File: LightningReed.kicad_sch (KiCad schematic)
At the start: 175 parts, among them P1 Conn_WallPlug, Q1 NCE65T180D, Q10 DMZ6005E, Q11 2N7002K, Q12 NCEP15T14D, Q13 BSS123, Q2 2N7002, Q3 1N60G, Q4 2N7002, Q5 2N7002K, Q6 2N7002K, Q7 NCE65T260K, Q8 NCE65T260K, Q9 NCE0102, T1 Transformer_2P_2S, U1 UCC28056, U2 78L05S, U3 LMC7111, U4 UCC28780, U5 UCC27712, U6 LM317G, U7 FODM8801A, U8 TL431DBZ, U9 UCC24612-1DBV

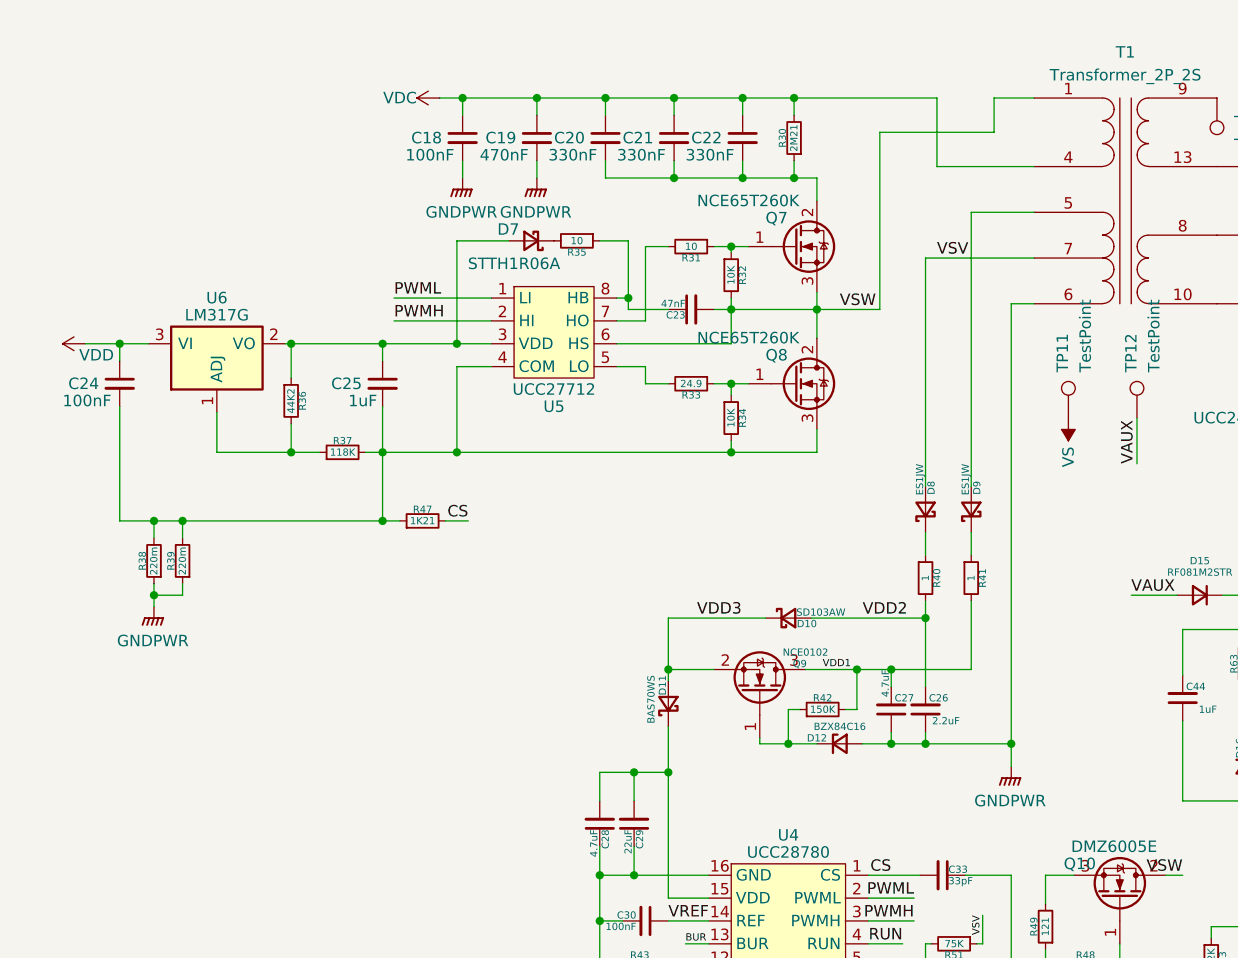
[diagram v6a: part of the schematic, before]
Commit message: Flyback controller left - layout
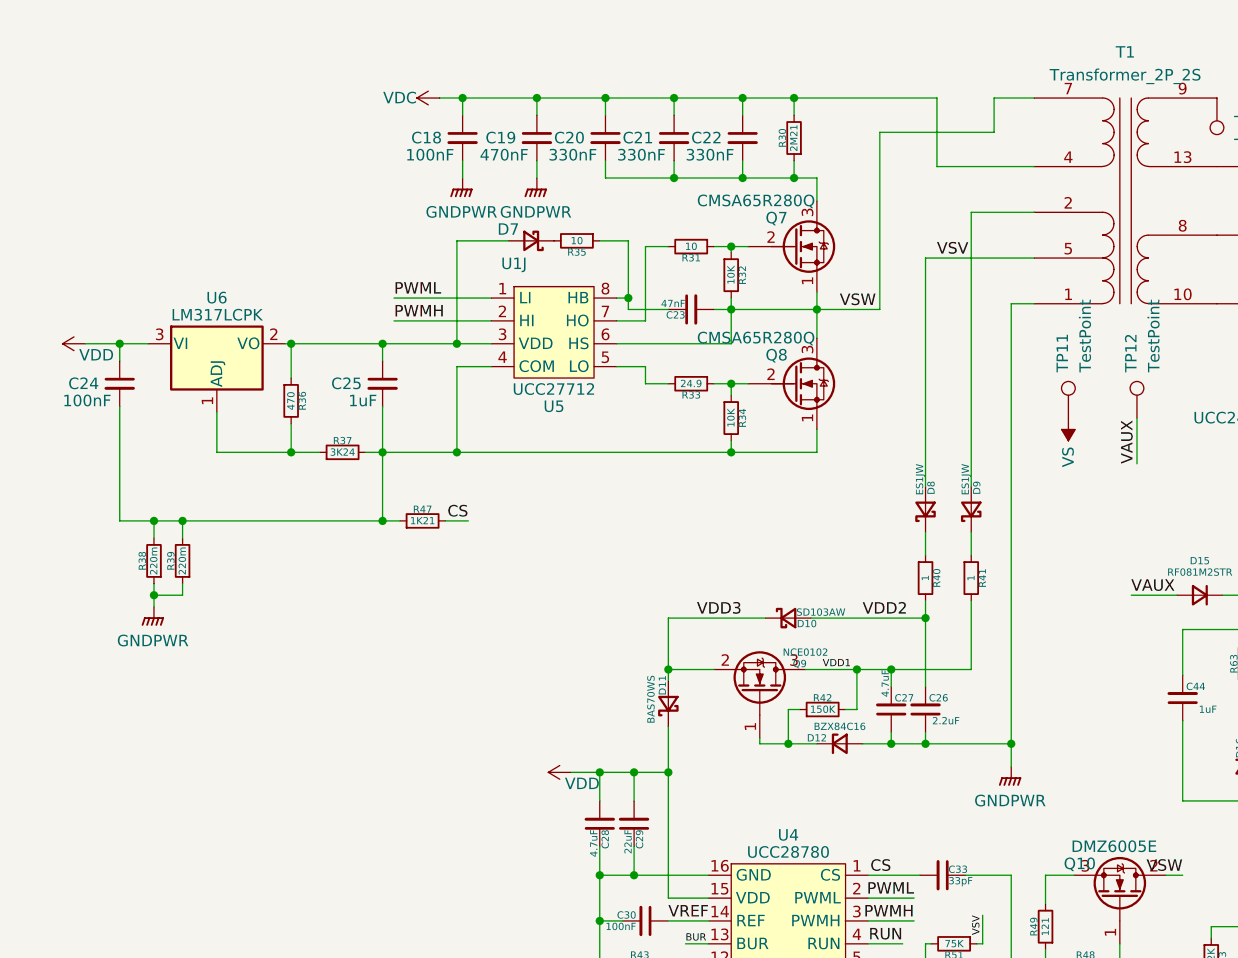
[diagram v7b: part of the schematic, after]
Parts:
- removed Q7: NCE65T260K, Package_TO_SOT_SMD:TO-252-2, symbol Device:Q_NMOS_GDS
- added Q7: CMSA65R280Q, Package_SON:VSONP-8-1EP_5x6_P1.27mm, symbol Device:Q_NMOS_SGD
- D7: value STTH1R06A -> U1J; footprint Diode_SMD:D_SMA -> Diode_SMD:D_SOD-123F
- Q8: value NCE65T260K -> CMSA65R280Q; footprint Package_TO_SOT_SMD:TO-252-2 -> Package_SON:VSONP-8-1EP_5x6_P1.27mm; symbol Device:Q_NMOS_GDS -> Device:Q_NMOS_SGD
- R36: value 44K2 -> 470
- R37: value 118K -> 3K24
- U2: footprint Package_TO_SOT_SMD:SOT-89-3 -> Package_TO_SOT_SMD:SOT-23
- U6: value LM317G -> LM317LCPK; footprint Package_TO_SOT_SMD:SOT-223-3_TabPin2 -> Package_TO_SOT_SMD:SOT-89-3; symbol Regulator_Linear:NCP1117-ADJ_SOT223 -> Regulator_Linear:LM317L_SOT-89
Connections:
- net GNDPWR: now also T1.1 (SD); no longer T1.6 (SD)
- net VDD: now also C28.2, C29.2, D11.1 (K), U4.15 (VDD)
- net VSV: now also T1.5 (SD); no longer T1.7 (SD)
- net VSW: now also Q8.3 (D), T1.7 (AA), Q7.1 (S); no longer Q8.2 (D), T1.1 (AA)
- net at R33.1, R34.1: now also Q8.2 (G); no longer Q8.1 (G)
- net at C24.2, C25.2, R34.2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: now also Q8.1 (S); no longer Q8.3 (S)
- net at C20.2, C21.2, C22.2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: now also Q7.3 (D)
- net at D9.2 (A): now also T1.2 (SC); no longer T1.5 (SC)
- net at R31.1, R32.1: now also Q7.2 (G)
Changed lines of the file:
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@@
   (junction (at 28.575 157.48) (diameter 0) (color 0 0 0 0)
   )
+  (junction (at 199.39 98.425) (diameter 0) (color 0 0 0 0)
+  )
   (junction (at 175.26 50.8) (diameter 0) (color 0 0 0 0)
   )
@@
     (stroke (width 0) (type default))
   )
+  (wire (pts (xy 196.215 98.425) (xy 199.39 98.425))
+    (stroke (width 0) (type default))
+  )
   (wire (pts (xy 271.145 78.74) (xy 271.145 82.55))
     (stroke (width 0) (type default))
@@
       (effects (font (size 1.27 1.27)))
     )
-    (property "Footprint" "Package_TO_SOT_SMD:SOT-89-3" (at 36.195 172.72 0)
+    (property "Footprint" "Package_TO_SOT_SMD:SOT-23" (at 36.195 172.72 0)
       (effects (font (size 1.27 1.27) italic) hide)
     )
@@
     )
   )
+  (symbol (lib_id "Device:Q_NMOS_SGD") (at 220.98 40.005 0) (unit 1)
+    (in_bom yes) (on_board yes) (dnp no)
+    (property "Reference" "Q7" (at 217.805 36.83 0)
+      (effects (font (size 1.27 1.27)) (justify left))
+    )
+    (property "Value" "CMSA65R280Q" (at 210.185 34.925 0)
+      (effects (font (size 1.27 1.27)) (justify left))
+    )
+    (property "Footprint" "Package_SON:VSONP-8-1EP_5x6_P1.27mm" (at 226.06 37.465 0)
+      (effects (font (size 1.27 1.27)) hide)
+    )
+    (property "Datasheet" "~" (at 220.98 40.005 0)
+      (effects (font (size 1.27 1.27)) hide)
+    )
+    (pin "1")
+    (pin "2")
+    (pin "3")
+    (instances
+      (project "LightningReed"
+        (path "/ed30a684-3009-4c45-ba04-268ec6465166"
+          (reference "Q7") (unit 1)
+        )
+      )
+    )
+  )
   (symbol (lib_id "Device:R_Small") (at 123.19 154.94 180) (unit 1)
     (in_bom yes) (on_board yes) (dnp no)
@@
     )
   )
+  (symbol (lib_id "power:VDD") (at 196.215 98.425 90) (unit 1)
+    (in_bom yes) (on_board yes) (dnp no)
+    (property "Reference" "#PWR042" (at 200.025 98.425 0)
+      (effects (font (size 1.27 1.27)) hide)
+    )
+    (property "Value" "VDD" (at 199.39 99.695 90)
+      (effects (font (size 1.27 1.27)) (justify left))
+    )
+    (property "Footprint" "" (at 196.215 98.425 0)
+      (effects (font (size 1.27 1.27)) hide)
+    )
+    (property "Datasheet" "" (at 196.215 98.425 0)
+      (effects (font (size 1.27 1.27)) hide)
+    )
+    (pin "1")
+    (instances
+      (project "LightningReed"
+        (path "/ed30a684-3009-4c45-ba04-268ec6465166"
+          (reference "#PWR042") (unit 1)
+        )
+      )
+    )
+  )
   (symbol (lib_id "Device:R_Small") (at 95.25 86.36 180) (unit 1)
     (in_bom yes) (on_board yes) (dnp no)
@@
       (effects (font (size 0.8 0.8)))
     )
-    (property "Value" "118K" (at 170.815 62.865 90)
+    (property "Value" "3K24" (at 170.815 62.865 90)
       (effects (font (size 0.8 0.8)))
     )
@@
       (effects (font (size 0.8 0.8)))
     )
-    (property "Value" "44K2" (at 165.1 57.15 90)
+    (property "Value" "470" (at 165.1 57.15 90)
       (effects (font (size 0.8 0.8)))
     )
@@
       (effects (font (size 1.27 1.27)) hide)
     )
-    (pin "1")
+    (pin "7")
     (pin "10")
     (pin "13")
     (pin "4")
+    (pin "2")
+    (pin "1")
     (pin "5")
-    (pin "6")
-    (pin "7")
     (pin "8")
     (pin "9")
@@
     )
   )
-  (symbol (lib_id "Device:Q_NMOS_GDS") (at 220.98 55.245 0) (unit 1)
+  (symbol (lib_id "Device:Q_NMOS_SGD") (at 220.98 55.245 0) (unit 1)
     (in_bom yes) (on_board yes) (dnp no)
     (property "Reference" "Q8" (at 217.805 52.07 0)
       (effects (font (size 1.27 1.27)) (justify left))
     )
-    (property "Value" "NCE65T260K" (at 210.185 50.165 0)
+    (property "Value" "CMSA65R280Q" (at 210.185 50.165 0)
       (effects (font (size 1.27 1.27)) (justify left))
     )
-    (property "Footprint" "Package_TO_SOT_SMD:TO-252-2" (at 226.06 52.705 0)
+    (property "Footprint" "Package_SON:VSONP-8-1EP_5x6_P1.27mm" (at 226.06 52.705 0)
       (effects (font (size 1.27 1.27)) hide)
     )
@@
       (effects (font (size 1.27 1.27)))
     )
-    (property "Value" "STTH1R06A" (at 189.865 41.91 0)
+    (property "Value" "U1J" (at 189.865 41.91 0)
       (effects (font (size 1.27 1.27)))
     )
-    (property "Footprint" "Diode_SMD:D_SMA" (at 191.77 39.37 90)
+    (property "Footprint" "Diode_SMD:D_SOD-123F" (at 191.77 39.37 90)
       (effects (font (size 1.27 1.27)) hide)
     )
@@
     )
   )
-  (symbol (lib_id "Regulator_Linear:NCP1117-ADJ_SOT223") (at 156.845 50.8 0) (unit 1)
+  (symbol (lib_id "Regulator_Linear:LM317L_SOT-89") (at 156.845 50.8 0) (unit 1)
     (in_bom yes) (on_board yes) (dnp no)
     (property "Reference" "U6" (at 156.845 45.72 0)
       (effects (font (size 1.27 1.27)))
     )
-    (property "Value" "LM317G" (at 156.845 47.625 0)
+    (property "Value" "LM317LCPK" (at 156.845 47.625 0)
       (effects (font (size 1.27 1.27)))
     )
-    (property "Footprint" "Package_TO_SOT_SMD:SOT-223-3_TabPin2" (at 156.845 45.72 0)
-      (effects (font (size 1.27 1.27)) hide)
+    (property "Footprint" "Package_TO_SOT_SMD:SOT-89-3" (at 156.845 44.45 0)
+      (effects (font (size 1.27 1.27) italic) hide)
     )
-    (property "Datasheet" "http://www.onsemi.com/pub_link/Collateral/NCP1117-D.PDF" (at 159.385 57.15 0)
+    (property "Datasheet" "http://www.ti.com/lit/ds/symlink/lm317l.pdf" (at 156.845 50.8 0)
       (effects (font (size 1.27 1.27)) hide)
     )
@@
         )
       )
-    )
-  )
-  (symbol (lib_id "Device:Q_NMOS_GDS") (at 220.98 40.005 0) (unit 1)
-    (in_bom yes) (on_board yes) (dnp no)
-    (property "Reference" "Q7" (at 217.805 36.83 0)
-      (effects (font (size 1.27 1.27)) (justify left))
-    )
-    (property "Value" "NCE65T260K" (at 210.185 34.925 0)
-      (effects (font (size 1.27 1.27)) (justify left))
-    )
-    (property "Footprint" "Package_TO_SOT_SMD:TO-252-2" (at 226.06 37.465 0)
-      (effects (font (size 1.27 1.27)) hide)
-    )
-    (property "Datasheet" "~" (at 220.98 40.005 0)
-      (effects (font (size 1.27 1.27)) hide)
-    )
-    (pin "1")
-    (pin "2")
-    (pin "3")
-    (instances
-      (project "LightningReed"
-        (path "/ed30a684-3009-4c45-ba04-268ec6465166"
-          (reference "Q7") (unit 1)
-        )
-      )

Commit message: Controller 50%
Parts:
- removed Q7: CMSA65R280Q, Package_SON:VSONP-8-1EP_5x6_P1.27mm, symbol Device:Q_NMOS_SGD
- removed TP10, TP11, TP12, TP13, TP14, TP15, TP16, TP9: TestPoint, Connector_Wire:SolderWire-0.15sqmm_1x01_D0.5mm_OD1.5mm, symbol Connector:TestPoint
- removed TP5, TP6, TP7, TP8: TestPoint, Connector_Wire:SolderWire-1sqmm_1x01_D1.4mm_OD2.7mm, symbol Connector:TestPoint
- added Q7: NCE65T260K, Package_TO_SOT_SMD:TO-252-2, symbol Device:Q_NMOS_GDS
- D7: value U1J -> STTH1R06A; footprint Diode_SMD:D_SOD-123F -> Diode_SMD:D_SMA
- Q8: value CMSA65R280Q -> NCE65T260K; footprint Package_SON:VSONP-8-1EP_5x6_P1.27mm -> Package_TO_SOT_SMD:TO-252-2; symbol Device:Q_NMOS_SGD -> Device:Q_NMOS_GDS
- R36: value 470 -> 44K2
- R37: value 3K24 -> 118K
- TP1: footprint Connector_Wire:SolderWire-1sqmm_1x01_D1.4mm_OD2.7mm -> Connector_Wire:SolderWire-0.5sqmm_1x01_D0.9mm_OD2.1mm
- U2: footprint Package_TO_SOT_SMD:SOT-23 -> Package_TO_SOT_SMD:SOT-89-3
- U6: value LM317LCPK -> LM317G; footprint Package_TO_SOT_SMD:SOT-89-3 -> Package_TO_SOT_SMD:SOT-223-3_TabPin2; symbol Regulator_Linear:LM317L_SOT-89 -> Regulator_Linear:NCP1117-ADJ_SOT223
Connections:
- net GNDPWR: now also T1.6 (SD), U7.3; no longer T1.1 (SD)
- net GNDS: now also T1.13 (SB)
- net VAUX: now also T1.8 (SC)
- net VDD: no longer C28.2, C29.2, D11.1 (K), U4.15 (VDD)
- net VS: now also T1.10 (SD)
- net VSV: now also T1.7 (SD); no longer T1.5 (SD)
- net VSW: now also Q8.2 (D), T1.1 (AA), Q7.3 (S); no longer Q8.3 (D), T1.7 (AA)
- net at R31.1, R32.1: now also Q7.1 (G)
- net at C20.2, C21.2, C22.2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: now also Q7.2 (D)
- net at R33.1, R34.1: now also Q8.1 (G); no longer Q8.2 (G)
- net at C24.2, C25.2, R34.2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: now also Q8.3 (S); no longer Q8.1 (S)
- net at R52.1: now also U7.4
- net at C38.1, Q12.3 (S), U9.2 (VS): now also T1.9 (SA)
- net at D9.2 (A): now also T1.5 (SC); no longer T1.2 (SC)
- new net: C28.2, C29.2, D11.1 (K), U4.15 (VDD)
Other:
- moved on the sheet: C35, C36, C37, R54, R55, R56, R57, R58, R59, R60, TP1, TP2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
